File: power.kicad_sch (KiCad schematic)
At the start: 39 parts, among them J1 Conn_01x04, J9 Conn_01x02, Q1 Q_NMOS, Q2 Q_NMOS, SW1 SW_SPST, U2 BQ77905, U5 LDL212PV33R

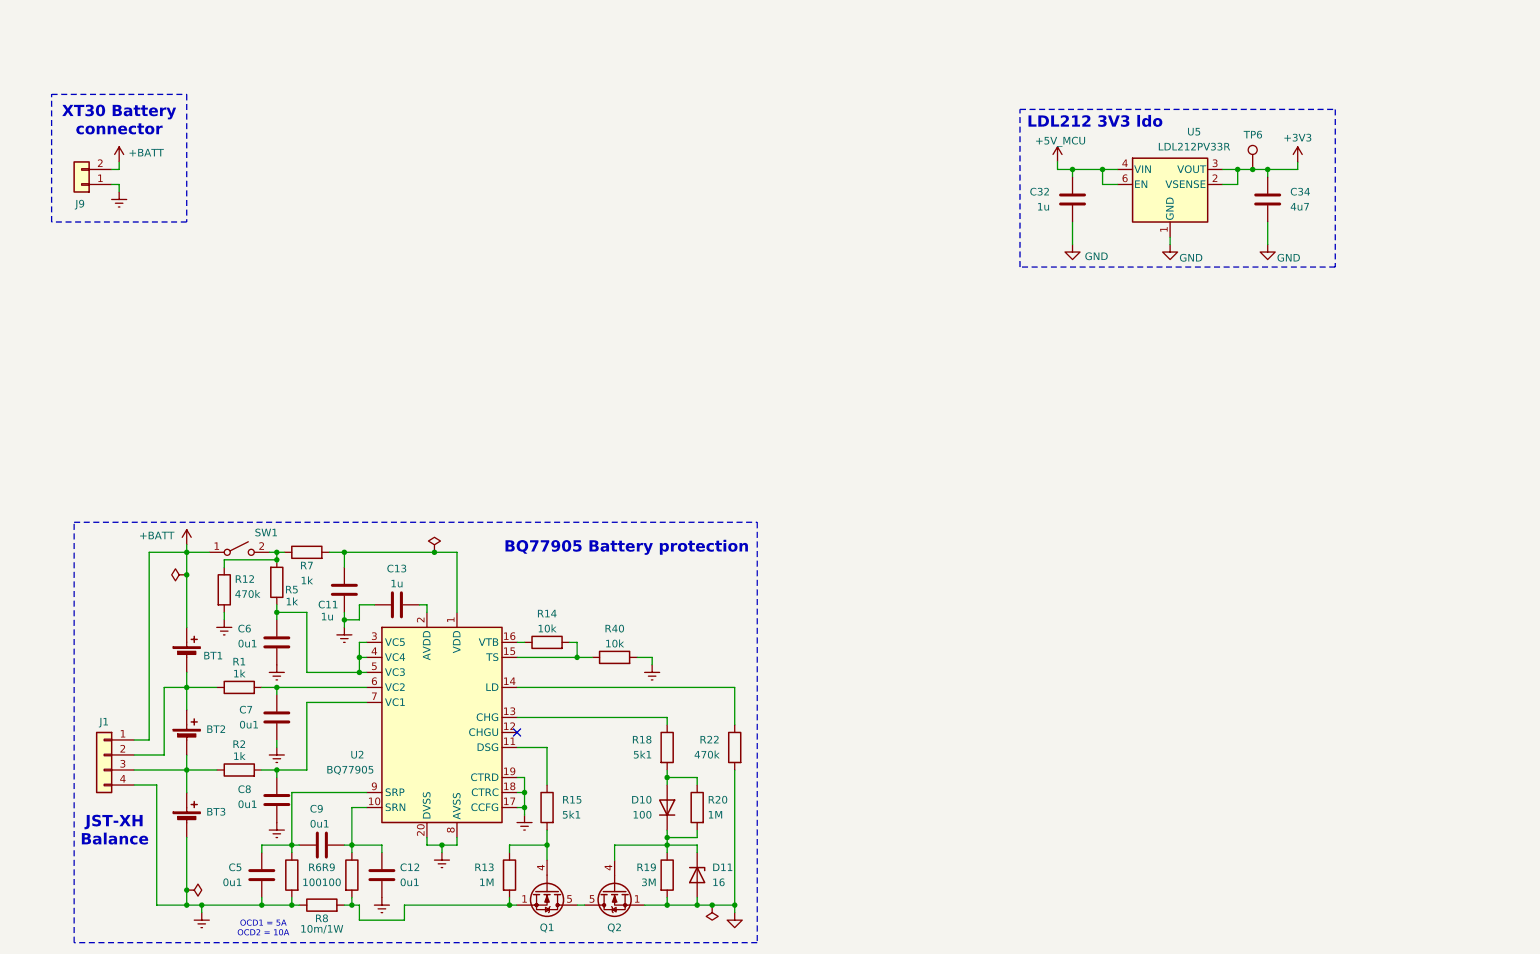
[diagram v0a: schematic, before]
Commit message: schem: add TPS62933 5V SMPS
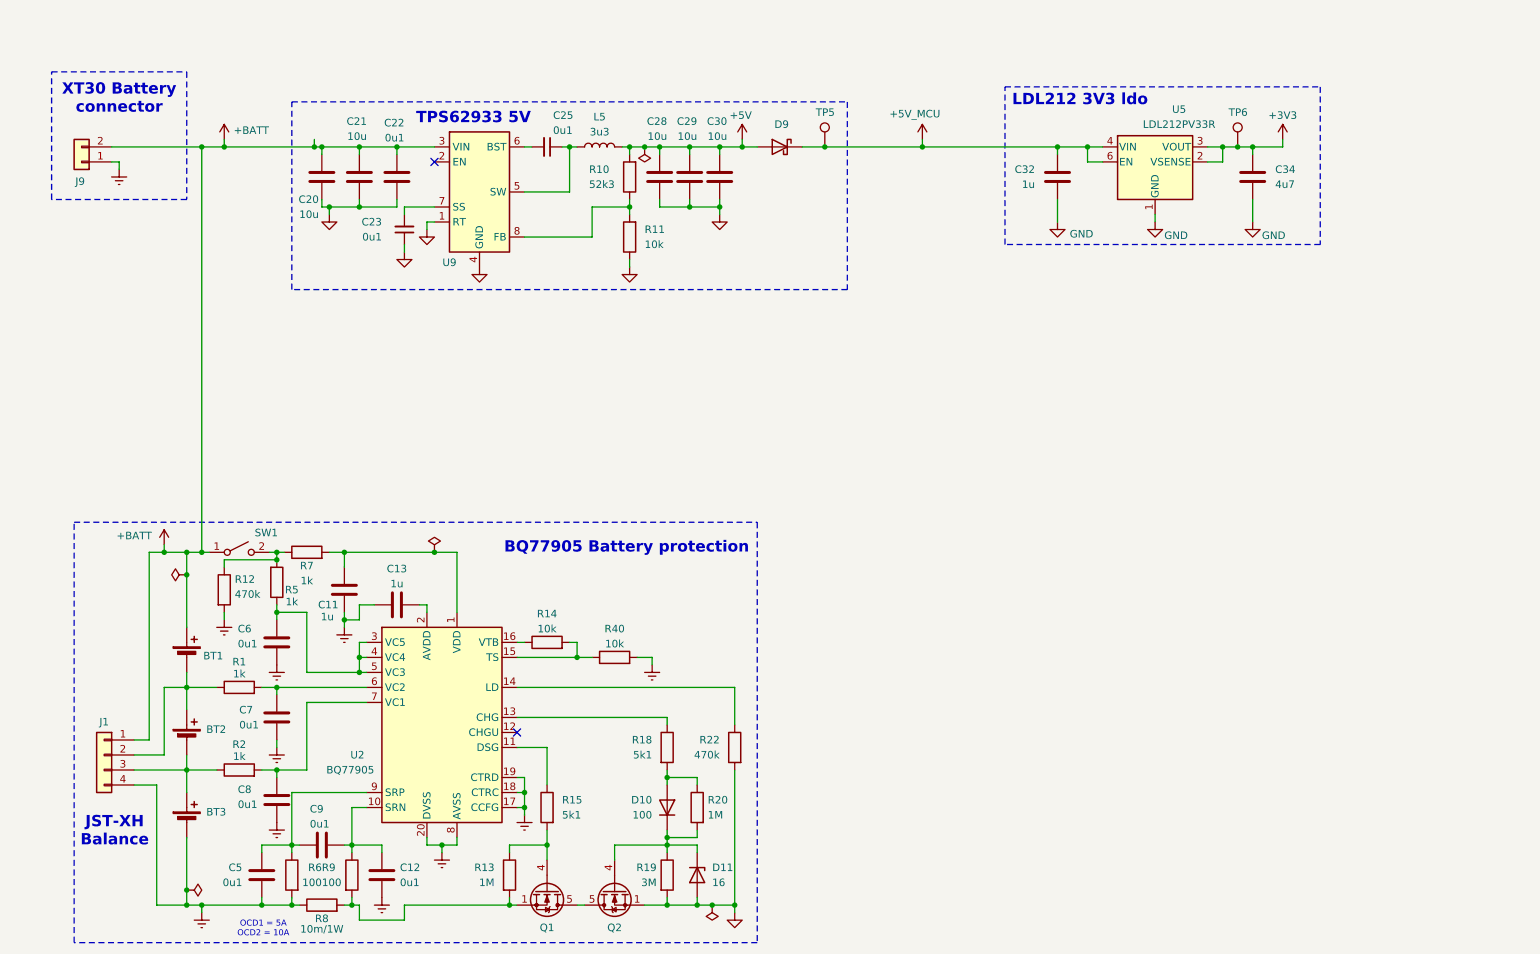
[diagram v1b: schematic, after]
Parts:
- added C20, C21, C28, C29, C30: 10u, Capacitor_SMD:C_0805_2012Metric, symbol Device:C
- added C22: 0u1, Capacitor_SMD:C_0402_1005Metric, symbol Device:C
- added C23, C25: 0u1, Capacitor_SMD:C_0402_1005Metric, symbol Device:C_Small
- added D9: D_Schottky, Diode_SMD:D_SMA, symbol Device:D_Schottky
- added L5: 3u3, Inductor_SMD:L_Sunlord_MWSA0402S, symbol Device:L
- added R10: 52k3, Resistor_SMD:R_0402_1005Metric, symbol Device:R
- added R11: 10k, Resistor_SMD:R_0402_1005Metric, symbol Device:R
- added TP5: TestPoint, TestPoint:TestPoint_Pad_D2.0mm, symbol Connector:TestPoint
- added U9: TPS62933, Package_TO_SOT_SMD:SOT-583-8, symbol Regulator_Switching:TPS62933
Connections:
- net +5V_MCU: now also D9.1 (K), TP5.1
- net +BATT: now also C20.1, C21.1, C22.1, U9.3 (VIN)
- net GND: now also C20.2, C21.2, C22.2, C23.1, C28.2, C29.2, C30.2, R11.1, U9.1 (RT), U9.4 (GND)
- new net: C23.2, U9.7 (SS)
- new net: R10.1, R11.2, U9.8 (FB)
- new net: C25.1, L5.1, U9.5 (SW)
- new net: C25.2, U9.6 (BST)
- new net +5V: C28.1, C29.1, C30.1, D9.2 (A), L5.2, R10.2
- no-connect marks 1 -> 2
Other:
- note added: "TPS62933 5V"
- moved on the sheet: C32, C34, J9, TP6, U5

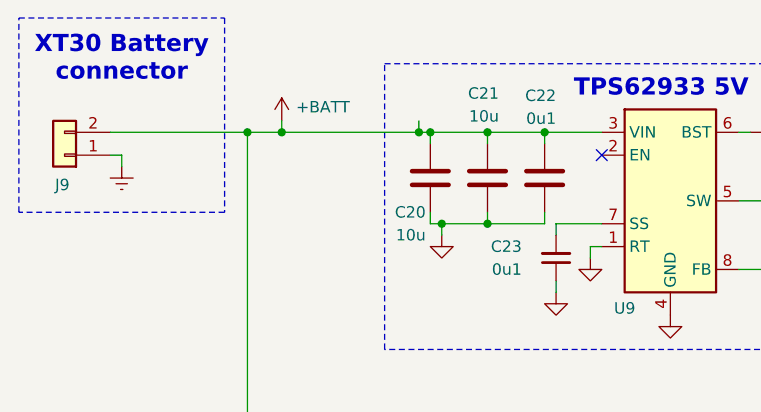
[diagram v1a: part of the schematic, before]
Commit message: schem: fix VDD_SPI cap
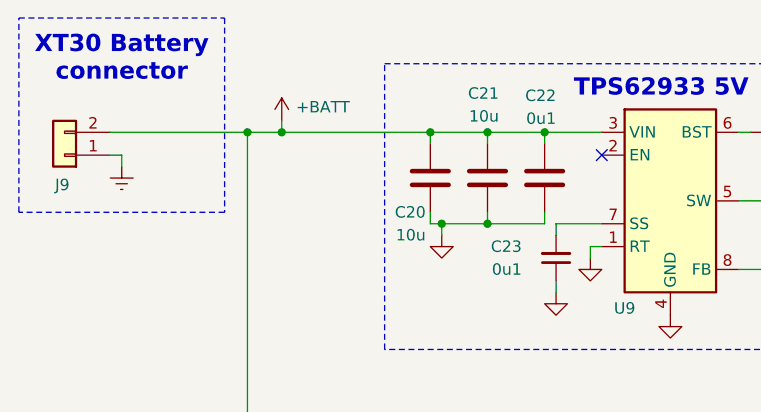
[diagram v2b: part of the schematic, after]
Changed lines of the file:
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@@
-	)
-	(junction
-		(at 71.12 55.88)
-		(diameter 0)
-		(color 0 0 0 0)
 	)
 	(junction
@@
 	(wire
 		(pts
-			(xy 71.12 54.61) (xy 71.12 55.88)
-		)
-		(stroke
-			(width 0)
-			(type default)
-		)
-	)
-	(wire
-		(pts
-			(xy 55.88 55.88) (xy 71.12 55.88)
-		)
-		(stroke
-			(width 0)
-			(type default)
-		)
-	)
-	(wire
-		(pts
 			(xy 78.74 144.78) (xy 80.01 144.78)
 		)
@@
 	(wire
 		(pts
-			(xy 71.12 55.88) (xy 72.39 55.88)
-		)
-		(stroke
+			(xy 55.88 55.88) (xy 72.39 55.88)
+		)
+		(stroke

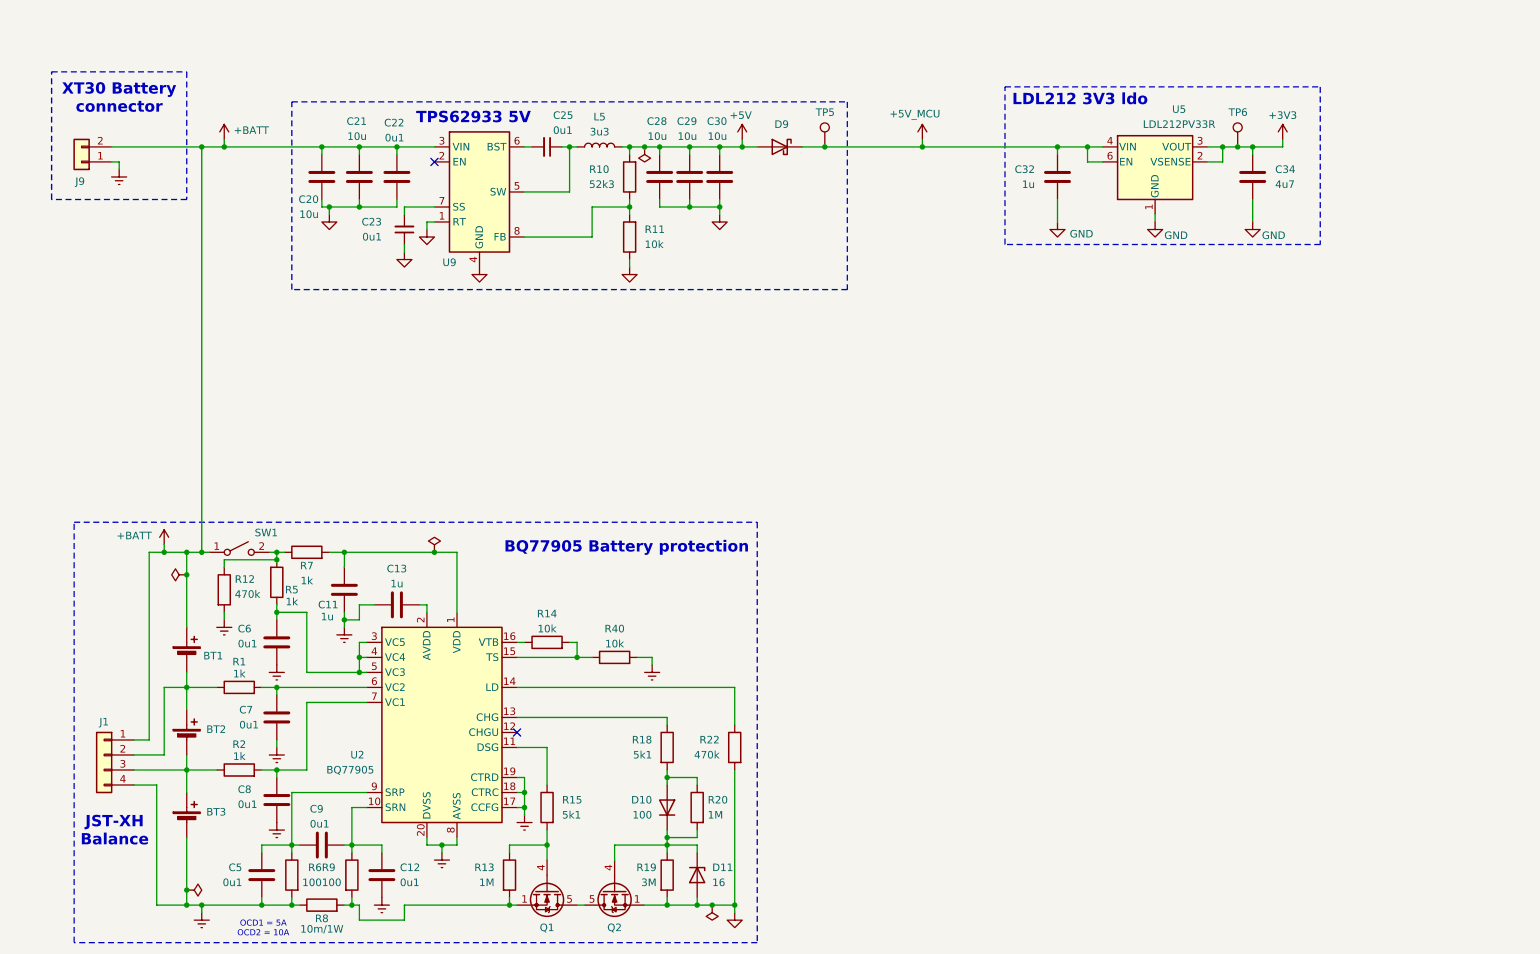
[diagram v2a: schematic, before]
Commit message: schem: add rain/wind schmitt trigger
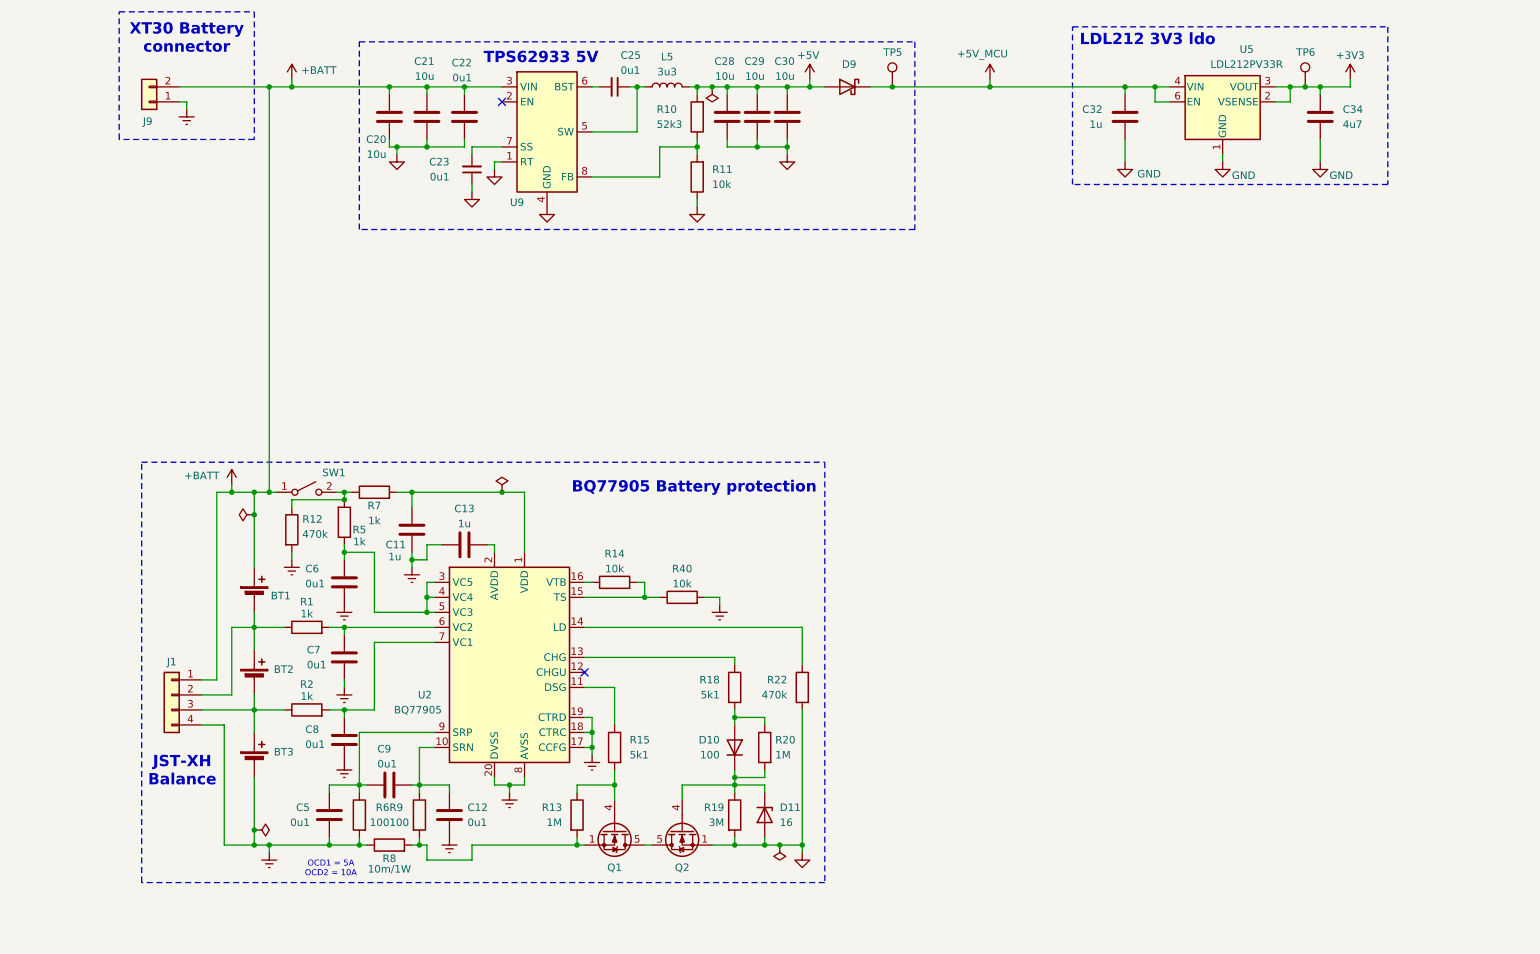
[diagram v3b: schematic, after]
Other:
- moved on the sheet: BT1, BT2, BT3, C11, C12, C13, C20, C21, C22, C23, C25, C28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

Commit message: schem: remove 3s BMS
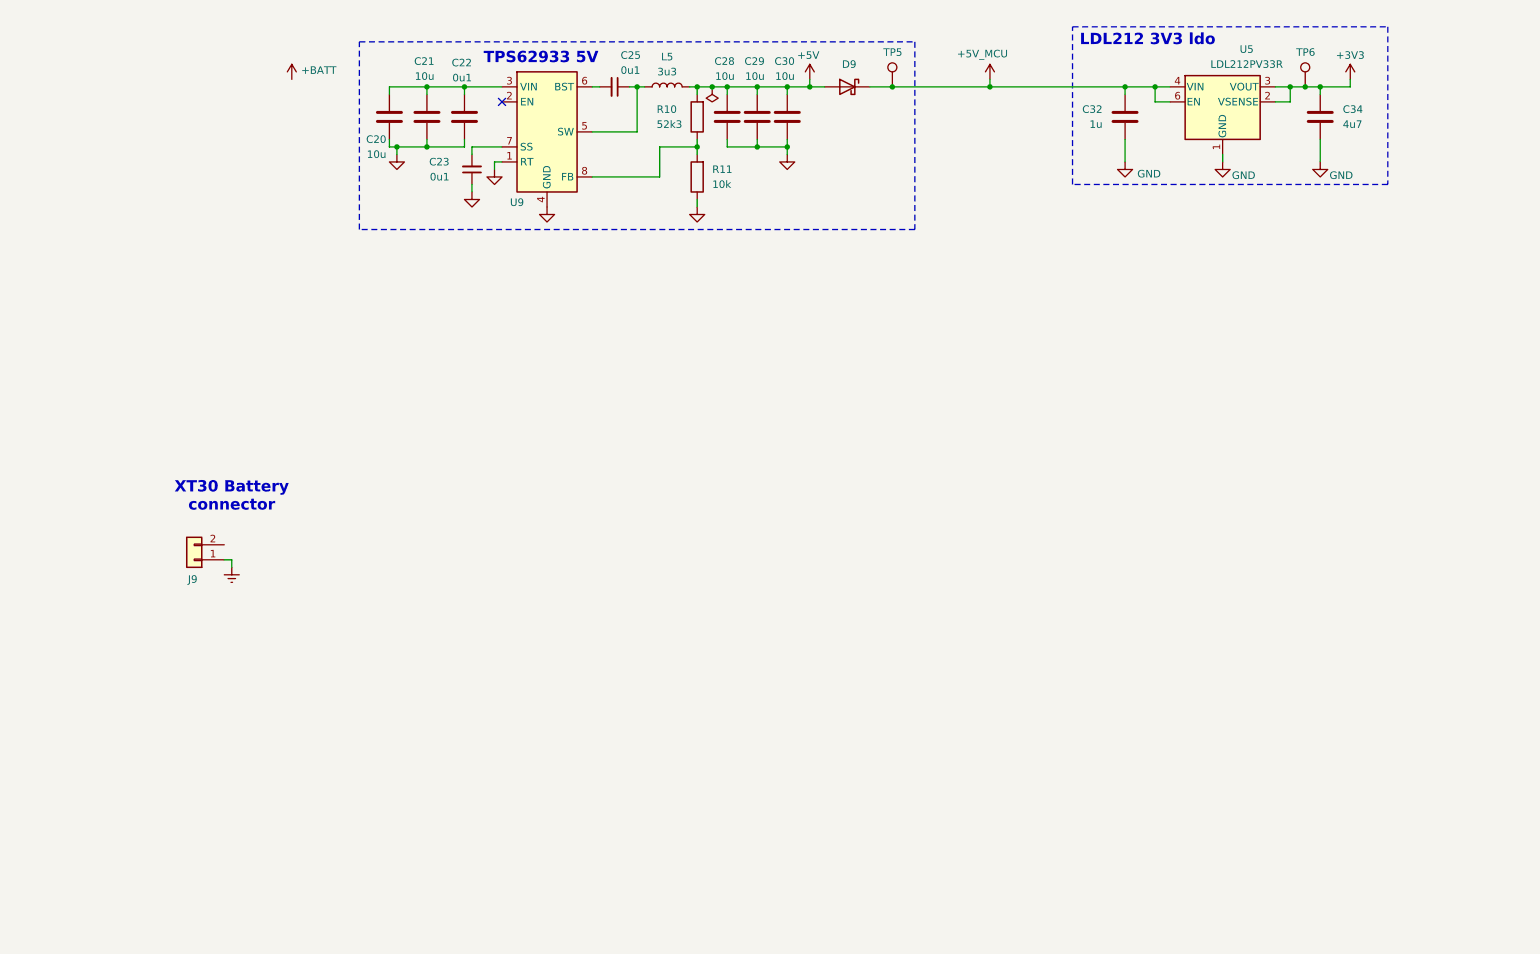
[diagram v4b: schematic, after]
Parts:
- removed BT1, BT2, BT3: Battery_Cell, symbol Device:Battery_Cell
- removed C11, C13: 1u, Capacitor_SMD:C_0402_1005Metric, symbol Device:C
- removed C12, C5, C6, C7, C8, C9: 0u1, Capacitor_SMD:C_0402_1005Metric, symbol Device:C
- removed D10: 100, Diode_SMD:D_SOD-323, symbol Device:D
- removed D11: 16, Diode_SMD:D_SOD-123, symbol Device:D_Zener
- removed J1: Conn_01x04, Connector_JST:JST_XH_S4B-XH-A_1x04_P2.50mm_Horizontal, symbol Connector_Generic:Conn_01x04
- removed Q1, Q2: Q_NMOS, Package_SO:Vishay_PowerPAK_1212-8_Single, symbol Transistor_FET:SiS454DN
- removed R1, R2, R5, R7: 1k, Resistor_SMD:R_0402_1005Metric, symbol Device:R
- removed R12, R22: 470k, Resistor_SMD:R_0603_1608Metric, symbol Device:R
- removed R13, R20: 1M, Resistor_SMD:R_0402_1005Metric, symbol Device:R
- removed R14, R40: 10k, Resistor_SMD:R_0402_1005Metric, symbol Device:R
- removed R15, R18: 5k1, Resistor_SMD:R_0402_1005Metric, symbol Device:R
- removed R19: 3M, Resistor_SMD:R_0603_1608Metric, symbol Device:R
- removed R6, R9: 100, Resistor_SMD:R_0402_1005Metric, symbol Device:R
- removed R8: 10m/1W, Resistor_SMD:R_1206_3216Metric, symbol Device:R
- removed SW1: SW_SPST, Connector_PinHeader_2.54mm:PinHeader_1x02_P2.54mm_Vertical, symbol Switch:SW_SPST
- removed U2: BQ77905, Package_SO:TSSOP-20_4.4x6.5mm_P0.65mm, symbol GLCS:BQ77905
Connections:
- net +BATT: no longer C20.1, C21.1, C22.1, J9.2 (Pin_2), U9.3 (VIN)
- new net: C20.1, C21.1, C22.1, U9.3 (VIN)
- no-connect marks 2 -> 1
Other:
- note removed: "BQ77905 Battery protection"
- note removed: "JST-XH Balance"
- note removed: "OCD1 = 5A OCD2 = 10A"
- moved on the sheet: J9
